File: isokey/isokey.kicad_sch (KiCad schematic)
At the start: 1 part, among them U1 BlackPill_STLINK

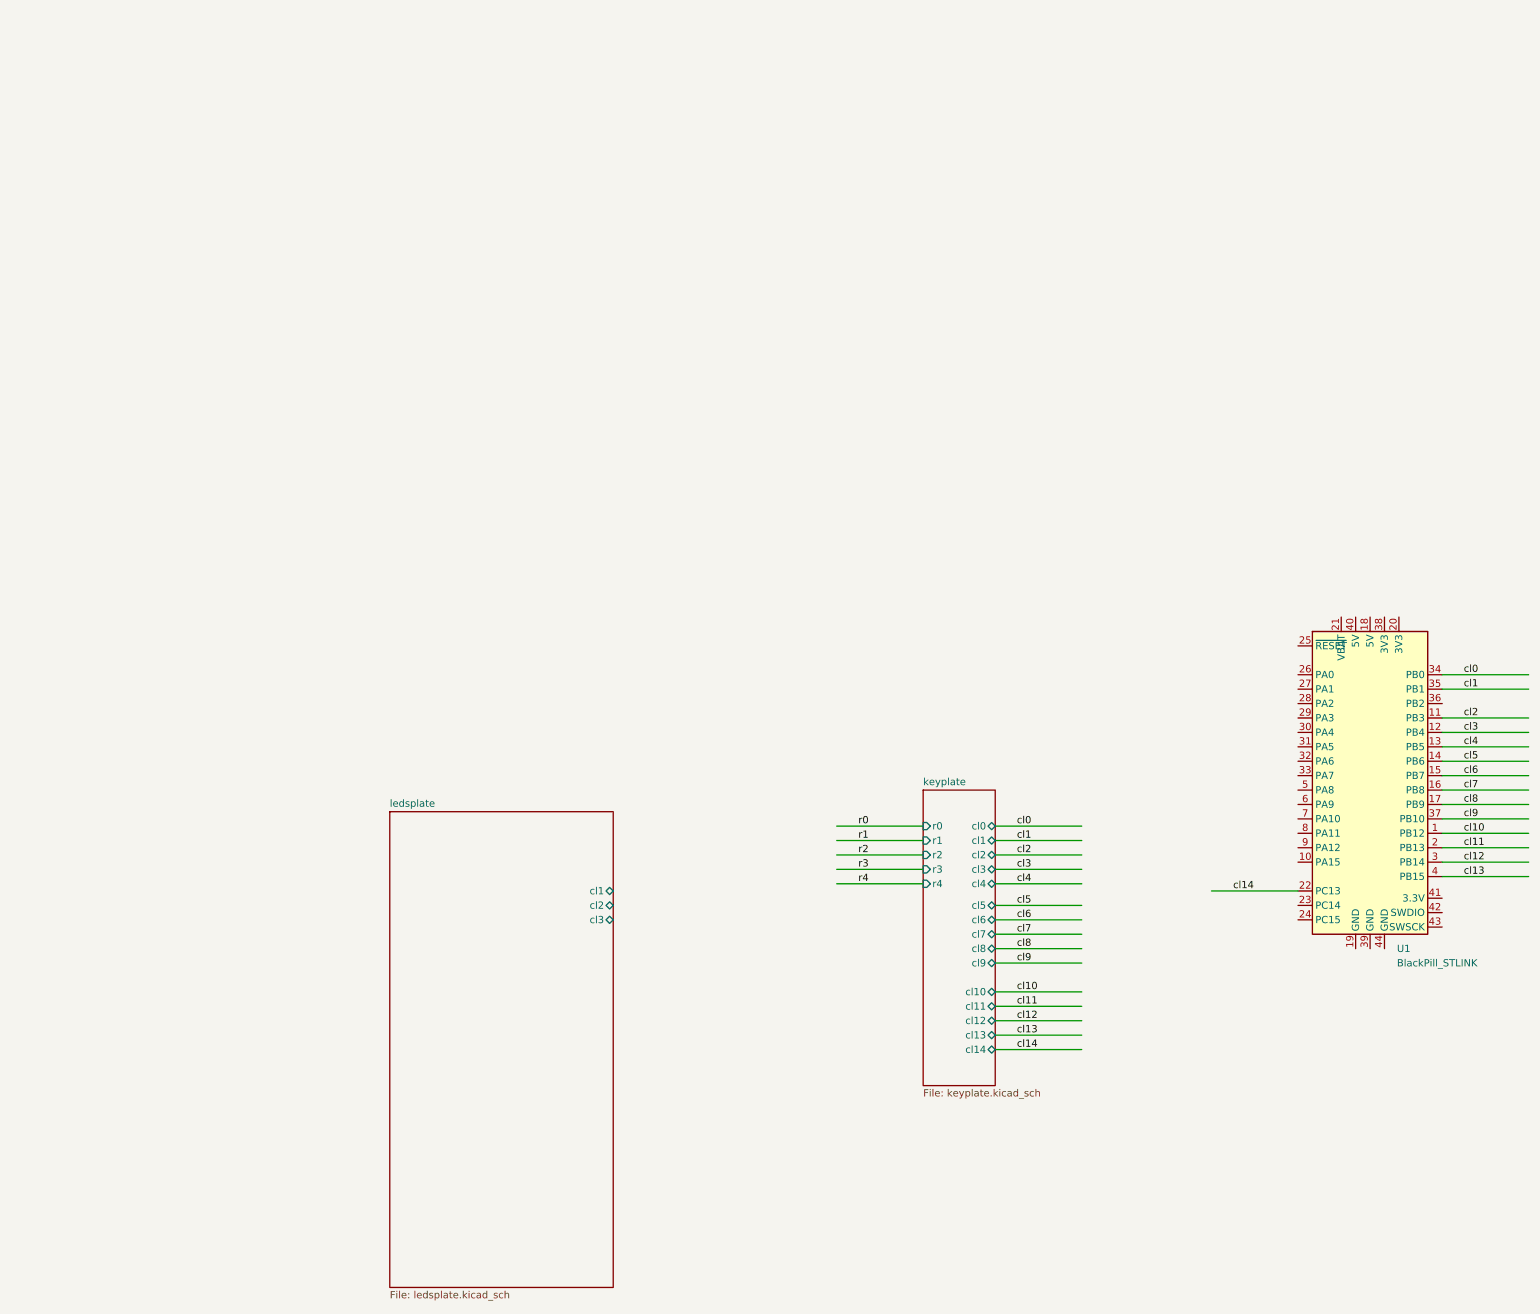
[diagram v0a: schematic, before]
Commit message: Add leds and extra connectors
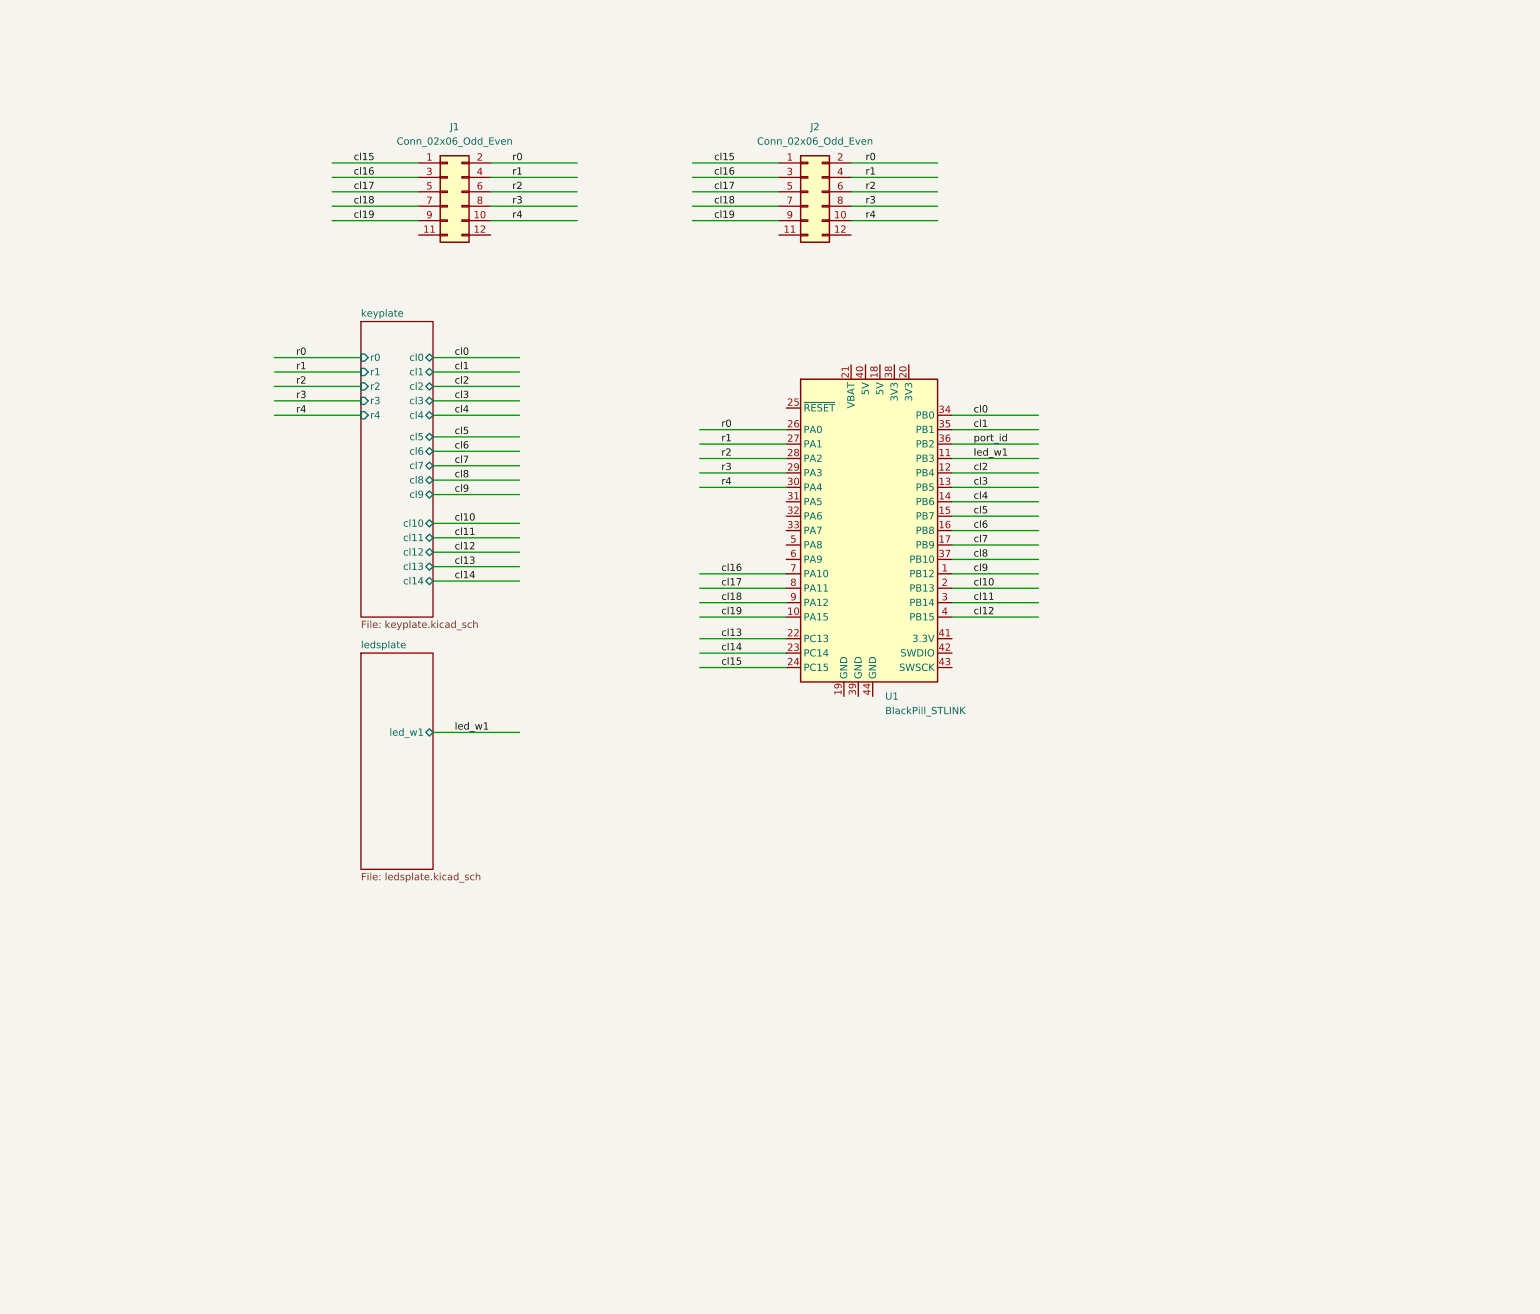
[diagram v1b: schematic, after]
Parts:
- added J1, J2: Conn_02x06_Odd_Even, symbol Connector_Generic:Conn_02x06_Odd_Even
- U1: footprint Modules:BlackPill_STLINK -> blackpill:BlackPill_STLINK
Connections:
- net cl10: now also U1.2 (PB13); no longer U1.1 (PB12)
- net cl11: now also U1.3 (PB14); no longer U1.2 (PB13)
- net cl12: now also U1.4 (PB15); no longer U1.3 (PB14)
- net cl13: now also U1.22 (PC13); no longer U1.4 (PB15)
- net cl14: now also U1.23 (PC14); no longer U1.22 (PC13)
- net cl2: now also U1.12 (PB4); no longer U1.11 (PB3)
- net cl3: now also U1.13 (PB5); no longer U1.12 (PB4)
- net cl4: now also U1.14 (PB6); no longer U1.13 (PB5)
- net cl5: now also U1.15 (PB7); no longer U1.14 (PB6)
- net cl6: now also U1.16 (PB8); no longer U1.15 (PB7)
- net cl7: now also U1.17 (PB9); no longer U1.16 (PB8)
- net cl8: now also U1.37 (PB10); no longer U1.17 (PB9)
- net cl9: now also U1.1 (PB12); no longer U1.37 (PB10)
- net r0: now also U1.26 (PA0), J1.2 (Pin_2), J2.2 (Pin_2)
- net r1: now also U1.27 (PA1), J1.4 (Pin_4), J2.4 (Pin_4)
- net r2: now also U1.28 (PA2), J1.6 (Pin_6), J2.6 (Pin_6)
- net r3: now also U1.29 (PA3), J1.8 (Pin_8), J2.8 (Pin_8)
- net r4: now also U1.30 (PA4), J1.10 (Pin_10), J2.10 (Pin_10)
- net cl19: now reaches U1.10 (PA15)
- net cl19: now also J1.9 (Pin_9), J2.9 (Pin_9)
- net cl15: now reaches U1.24 (PC15)
- net cl15: now also J1.1 (Pin_1), J2.1 (Pin_1)
- net port_id: now reaches U1.36 (PB2)
- net cl16: now reaches U1.7 (PA10)
- net cl16: now also J1.3 (Pin_3), J2.3 (Pin_3)
- net cl17: now reaches U1.8 (PA11)
- net cl17: now also J1.5 (Pin_5), J2.5 (Pin_5)
- net cl18: now reaches U1.9 (PA12)
- net cl18: now also J1.7 (Pin_7), J2.7 (Pin_7)
- new net led_w1: U1.11 (PB3)
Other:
- sheet ledsplate ports: added led_w1; removed cl1, cl2, cl3

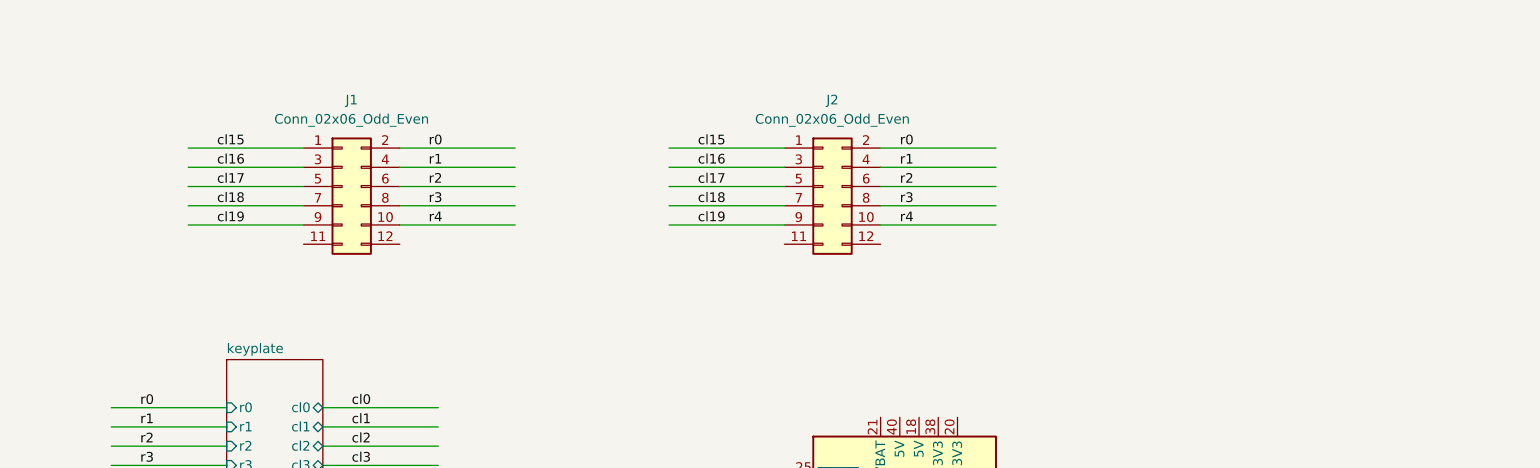
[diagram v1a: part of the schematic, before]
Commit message: Place switch and leds
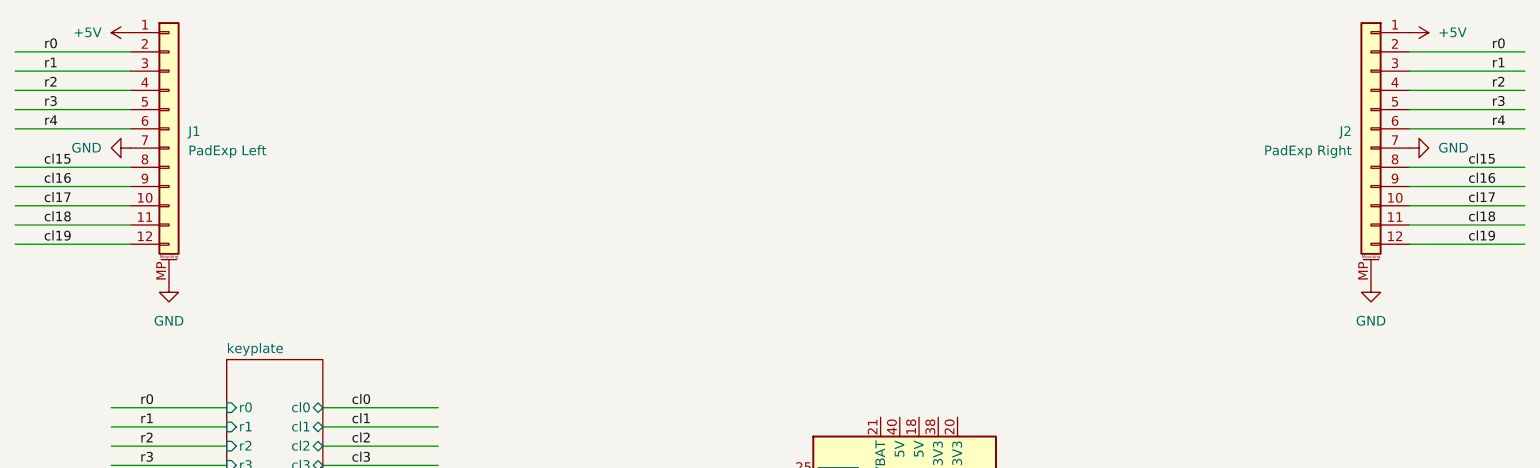
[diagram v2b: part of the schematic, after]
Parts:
- removed J1, J2: Conn_02x06_Odd_Even, symbol Connector_Generic:Conn_02x06_Odd_Even
- added J1: PadExp Left, Connector_JST:JST_GH_SM12B-GHS-TB_1x12-1MP_P1.25mm_Horizontal, symbol Connector_Generic_MountingPin:Conn_01x12_MountingPin
- added J2: PadExp Right, Connector_JST:JST_GH_SM12B-GHS-TB_1x12-1MP_P1.25mm_Horizontal, symbol Connector_Generic_MountingPin:Conn_01x12_MountingPin
- U1: footprint blackpill:BlackPill_STLINK -> Modules:BlackPill_STLINK
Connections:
- net cl15: now also J1.8 (Pin_8), J2.8 (Pin_8)
- net cl16: now also J1.9 (Pin_9), J2.9 (Pin_9)
- net cl17: now also J1.10 (Pin_10), J2.10 (Pin_10)
- net cl18: now also J1.11 (Pin_11), J2.11 (Pin_11)
- net cl19: now also J1.12 (Pin_12), J2.12 (Pin_12)
- net r0: now also J1.2 (Pin_2), J2.2 (Pin_2)
- net r1: now also J1.3 (Pin_3), J2.3 (Pin_3)
- net r2: now also J1.4 (Pin_4), J2.4 (Pin_4)
- net r3: now also J1.5 (Pin_5), J2.5 (Pin_5)
- net r4: now also J1.6 (Pin_6), J2.6 (Pin_6)
- new net +5V: J1.1 (Pin_1), J2.1 (Pin_1)
- new net GND: J1.7 (Pin_7), J1.MP (MountPin), J2.7 (Pin_7), J2.MP (MountPin)

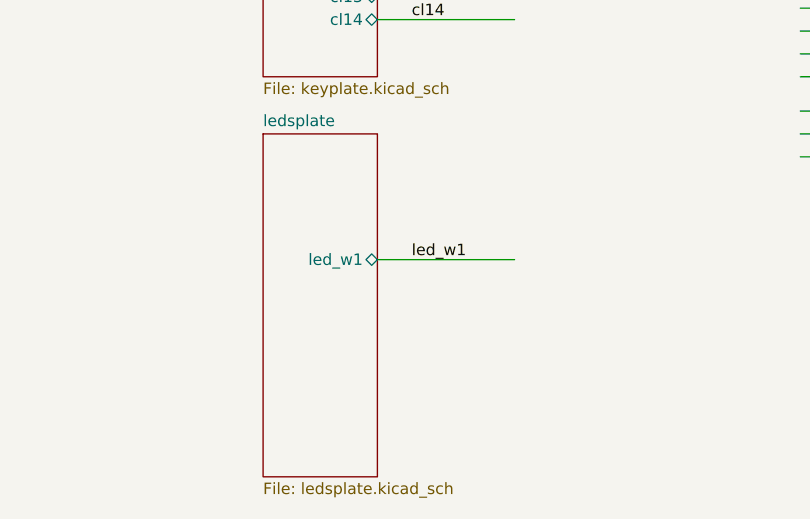
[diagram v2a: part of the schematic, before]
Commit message: Complete led wire
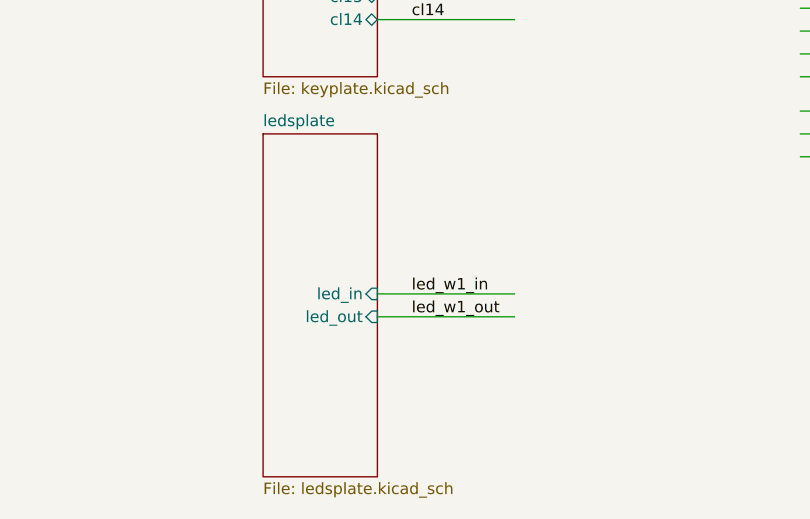
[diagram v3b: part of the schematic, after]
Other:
- sheet ledsplate ports: added led_in, led_out; removed led_w1
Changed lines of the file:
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@@
+    (stroke (width 0) (type default))
+  )
+  (wire (pts (xy 96.52 146.05) (xy 111.76 146.05))
     (stroke (width 0) (type default))
   )
@@
     (stroke (width 0) (type default))
   )
-  (wire (pts (xy 96.52 139.7) (xy 111.76 139.7))
+  (wire (pts (xy 96.52 143.51) (xy 111.76 143.51))
     (stroke (width 0) (type default))
   )
@@
     (effects (font (size 1.27 1.27)) (justify right bottom))
   )
-  (label "led_w1" (at 100.33 139.7 0) (fields_autoplaced)
+  (label "led_w1_in" (at 100.33 143.51 0) (fields_autoplaced)
     (effects (font (size 1.27 1.27)) (justify left bottom))
   )
@@
   )
   (label "r2" (at 72.39 78.74 0) (fields_autoplaced)
+    (effects (font (size 1.27 1.27)) (justify left bottom))
+  )
+  (label "led_w1_out" (at 100.33 146.05 0) (fields_autoplaced)
     (effects (font (size 1.27 1.27)) (justify left bottom))
   )
@@
       (effects (font (size 1.27 1.27)) (justify left top))
     )
-    (pin "led_w1" bidirectional (at 96.52 139.7 0)
+    (pin "led_in" input (at 96.52 143.51 0)
       (effects (font (size 1.27 1.27)) (justify right))
     )
+    (pin "led_out" input (at 96.52 146.05 0)
+      (effects (font (size 1.27 1.27)) (justify right))
+    )
